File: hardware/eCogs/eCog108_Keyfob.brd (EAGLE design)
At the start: 47.5 x 28 mm, 7 parts

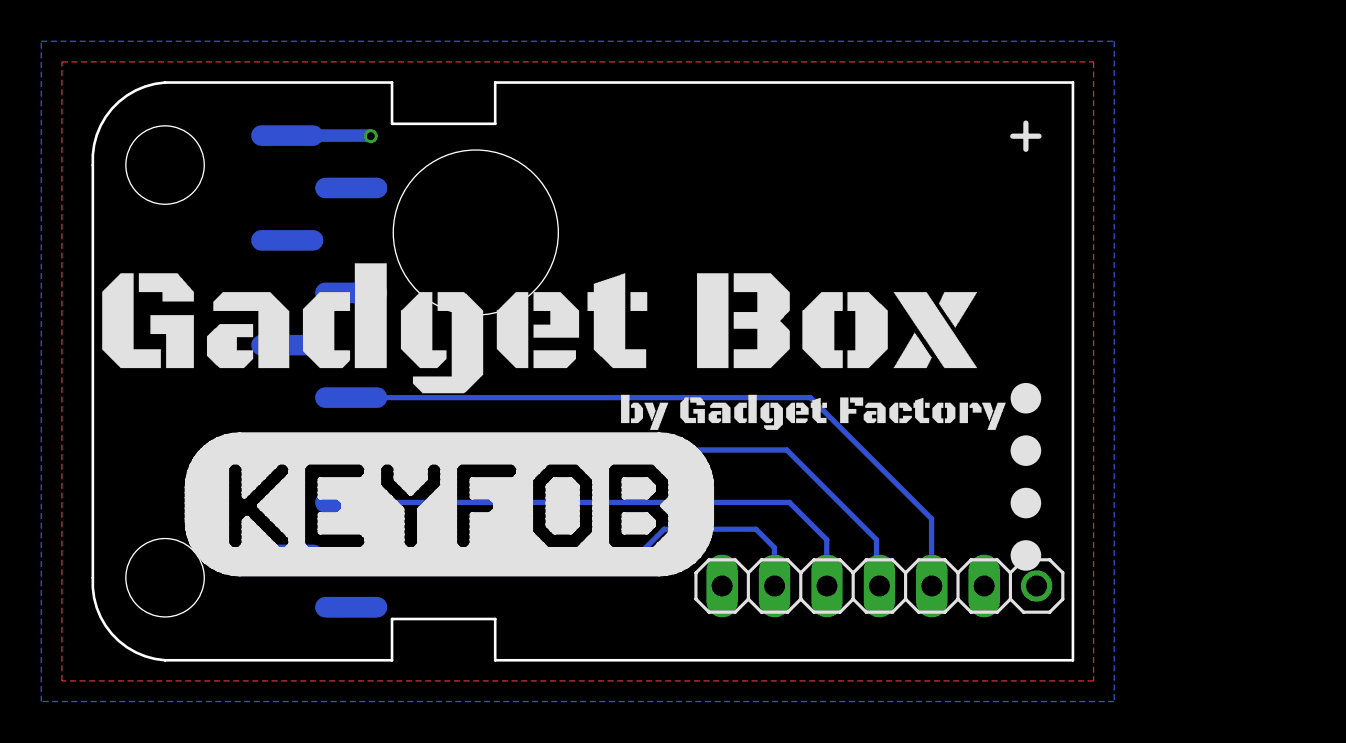
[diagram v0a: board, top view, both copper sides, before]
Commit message: Update eCogs to through hole
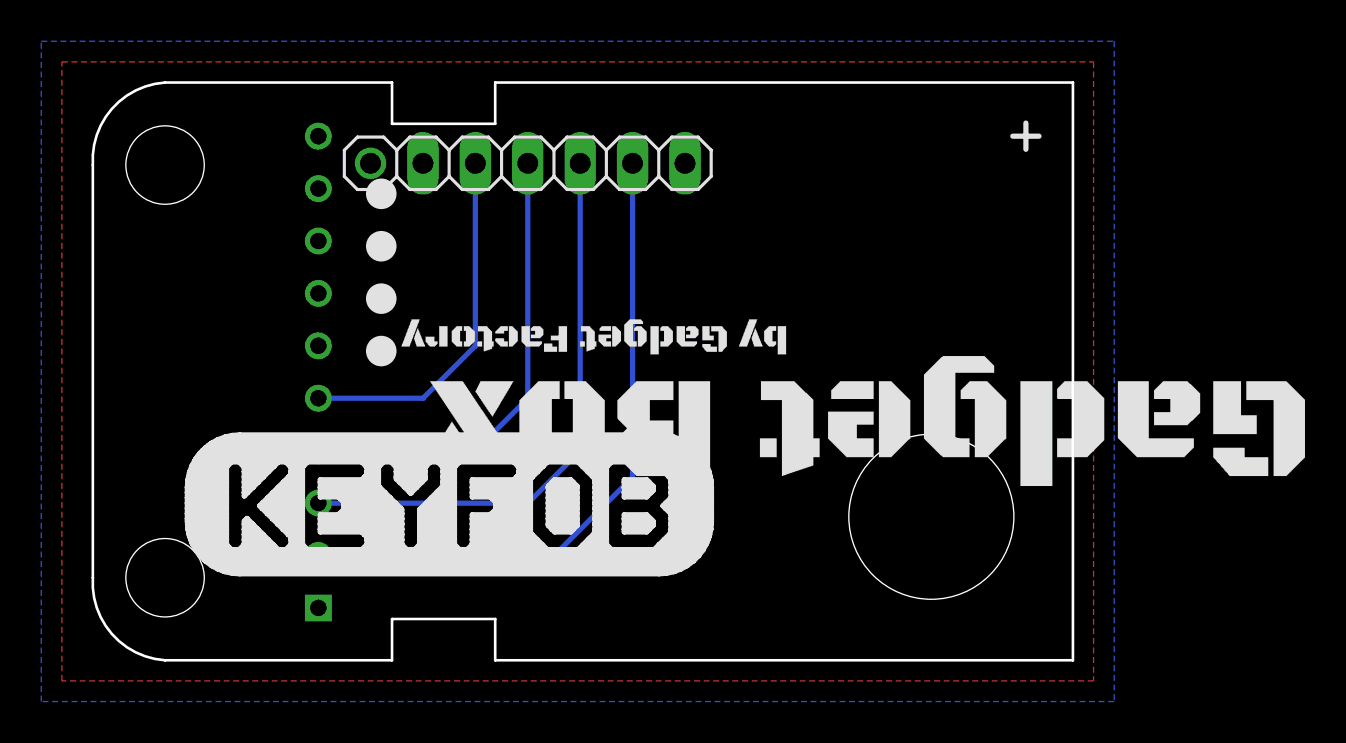
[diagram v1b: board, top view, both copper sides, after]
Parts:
- ECOG: value ECOG_GENERAL_ROWECOG_GENERAL_SMD -> ECOG_GENERAL_ROWTHROUGHOLE; device eCogs:ECOG_GENERAL_SMD -> eCogs:ECOG_GENERAL_TH
- moved U$5 35.8 mm to (14.5, 22.6), turned to 180 degrees
- moved U$4 33.6 mm to (14.5, 20.1), turned to 180 degrees
- moved U$3 32.1 mm to (14.5, 17.5), turned to 180 degrees
- moved U$2 31.3 mm to (14.5, 15.0), turned to 180 degrees
- moved JP1 26.6 mm to (21.6, 24.1), turned to 180 degrees
- moved U$1 16.3 mm to (38.0, 11.8), turned to 180 degrees
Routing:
- net D0: track 33.8 -> 17.5 mm
- net D1: track 32.7 -> 22.6 mm
- net D3: track 26.4 -> 32.0 mm
- net 3V3: track 4.06 -> 0.00 mm, vias 1 -> 0
- net D2: track 26.0 -> 27.7 mm
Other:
- board text added: "XC0"
- board text added: "XC1"
- board text added: "XC2"
- board text added: "XC3"
- board text added: "ecog108 v2.1"
- board text removed: "0"
- board text removed: "1"
- board text removed: "2"
- board text removed: "3"
- board text removed: "ecog108 v2.0"
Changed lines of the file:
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@@
 <layer number="19" name="Unrouted" color="6" fill="1" visible="yes" active="yes"/>
 <layer number="20" name="Dimension" color="15" fill="1" visible="yes" active="yes"/>
-<layer number="21" name="tPlace" color="16" fill="1" visible="yes" active="yes"/>
+<layer number="21" name="tPlace" color="16" fill="1" visible="no" active="yes"/>
 <layer number="22" name="bPlace" color="14" fill="1" visible="yes" active="yes"/>
 <layer number="23" name="tOrigins" color="15" fill="1" visible="yes" active="yes"/>
@@
 <board>
 <plain>
-<text x="43.909" y="22.225" size="0.8128" layer="22" font="vector" rot="MR0">ecog108.GadgetFactory.net</text>
-<text x="42.242" y="12.319" size="1.016" layer="22" font="vector" rot="MR0">ecog108 v2.0</text>
-<text x="42.242" y="13.589" size="1.016" layer="22" font="vector" rot="MR0">Keyfob</text>
-<text x="42.242" y="14.859" size="1.016" layer="22" font="vector" rot="MR0">eCogs</text>
-<text x="17.685" y="7.112" size="1.016" layer="22" font="vector" rot="MR0">D2</text>
-<text x="17.685" y="9.652" size="1.016" layer="22" font="vector" rot="MR0">D1</text>
-<text x="17.685" y="12.192" size="1.016" layer="22" font="vector" rot="MR0">D0</text>
-<text x="17.685" y="4.572" size="1.016" layer="22" font="vector" rot="MR0">D3</text>
-<text x="40.132" y="21.336" size="0.6096" layer="22" font="vector" rot="MR0">Copyright 2016</text>
-<text x="41.862" y="20.447" size="0.6096" layer="22" font="vector" rot="MR0">Gadget Factory, LLC</text>
+<text x="46.703" y="21.717" size="0.8128" layer="22" font="vector" rot="MR0">ecog108.GadgetFactory.net</text>
+<text x="45.036" y="11.811" size="1.016" layer="22" font="vector" rot="MR0">ecog108 v2.1</text>
+<text x="45.036" y="13.081" size="1.016" layer="22" font="vector" rot="MR0">Keyfob</text>
+<text x="45.036" y="14.351" size="1.016" layer="22" font="vector" rot="MR0">eCogs</text>
+<text x="9.938" y="6.985" size="1.016" layer="22" font="vector" rot="MR0">D2</text>
+<text x="9.938" y="9.525" size="1.016" layer="22" font="vector" rot="MR0">D1</text>
+<text x="9.938" y="12.065" size="1.016" layer="22" font="vector" rot="MR0">D0</text>
+<text x="9.938" y="4.445" size="1.016" layer="22" font="vector" rot="MR0">D3</text>
+<text x="42.926" y="20.828" size="0.6096" layer="22" font="vector" rot="MR0">Copyright 2016</text>
+<text x="44.656" y="19.939" size="0.6096" layer="22" font="vector" rot="MR0">Gadget Factory, LLC</text>
 <text x="8.541" y="26.289" size="1.016" layer="22" font="vector" rot="MR0">3.3V</text>
-<text x="17.685" y="2.413" size="1.016" layer="22" font="vector" rot="MR0">GND</text>
-<wire x1="6.06" y1="2" x2="47.06" y2="2" width="0.254" layer="22"/>
-<wire x1="47.06" y1="2" x2="47.06" y2="25" width="0.254" layer="22"/>
-<wire x1="47.06" y1="25" x2="6.06" y2="25" width="0.254" layer="22"/>
-<wire x1="6.06" y1="25" x2="6.06" y2="2" width="0.254" layer="22"/>
-<hole x="19.06" y="20.73" drill="8"/>
+<text x="9.938" y="2.286" size="1.016" layer="22" font="vector" rot="MR0">GND</text>
+<wire x1="54.138" y1="25.686" x2="13.138" y2="25.686" width="0.254" layer="22"/>
+<wire x1="13.138" y1="25.686" x2="13.138" y2="2.686" width="0.254" layer="22"/>
+<wire x1="13.138" y1="2.686" x2="54.138" y2="2.686" width="0.254" layer="22"/>
+<wire x1="54.138" y1="2.686" x2="54.138" y2="25.686" width="0.254" layer="22"/>
+<hole x="41.138" y="6.956" drill="8"/>
 <wire x1="23.6582" y1="6.2196" x2="22.8848" y2="6.2196" width="0.254" layer="21"/>
 <wire x1="22.8848" y1="6.2196" x2="22.7544" y2="6.35" width="0.254" layer="21"/>
@@
 <wire x1="6.1068" y1="10.414" x2="29.4532" y2="10.414" width="0.254" layer="21"/>
 <wire x1="6.52" y1="10.668" x2="29.04" y2="10.668" width="0.254" layer="21"/>
-<text x="7.906" y="4.572" size="1.016" layer="22" font="vector" rot="MR0">0</text>
+<text x="8.287" y="5.08" size="1.016" layer="22" font="vector" rot="MR0">XC0</text>
 <wire x1="45.72" y1="26.035" x2="45.72" y2="24.765" width="0.254" layer="21"/>
 <wire x1="45.085" y1="25.4" x2="46.355" y2="25.4" width="0.254" layer="21"/>
-<text x="7.906" y="7.112" size="1.016" layer="22" font="vector" rot="MR0">1</text>
-<text x="7.906" y="9.652" size="1.016" layer="22" font="vector" rot="MR0">2</text>
-<text x="7.906" y="12.192" size="1.016" layer="22" font="vector" rot="MR0">3</text>
+<text x="7.779" y="6.985" size="1.016" layer="22" font="vector" rot="MR0">XC1</text>
+<text x="7.779" y="9.525" size="1.016" layer="22" font="vector" rot="MR0">XC2</text>
+<text x="7.779" y="12.065" size="1.016" layer="22" font="vector" rot="MR0">XC3</text>
 </plain>
 <attributes>
@@
 </autorouter>
 <elements>
-<element name="ECOG" library="eCogs" package="ECOG_GENERAL_SMD" value="ECOG_GENERAL_ROWECOG_GENERAL_SMD" x="0" y="0" smashed="yes">
-<attribute name="DIGIKEY" value="S1013EC-10-ND" x="0" y="0" size="1.778" layer="27" display="off"/>
+<element name="ECOG" library="eCogs" package="ECOG_GENERAL_TH" value="ECOG_GENERAL_ROWTHROUGHOLE" x="0" y="0" smashed="yes"/>
+<element name="U$2" library="eCogs" package="LEGEND_DIO" value="" x="14.478" y="14.986" rot="R180"/>
+<element name="U$3" library="eCogs" package="LEGEND_DIO" value="" x="14.478" y="17.526" rot="R180"/>
+<element name="JP1" library="pinhead" package="1X07" value="" x="21.578" y="24.086" smashed="yes" rot="R180">
+<attribute name="VALUE" x="30.468" y="27.261" size="1.27" layer="27" rot="R180"/>
 </element>
-<element name="U$2" library="eCogs" package="LEGEND_DIO" value="" x="45.72" y="12.7"/>
-<element name="U$3" library="eCogs" package="LEGEND_DIO" value="" x="45.72" y="10.16"/>
-<element name="JP1" library="pinhead" package="1X07" value="" x="38.62" y="3.6" smashed="yes">
-<attribute name="VALUE" x="29.73" y="0.425" size="1.27" layer="27"/>
-</element>
-<element name="U$4" library="eCogs" package="LEGEND_DIO" value="" x="45.72" y="7.62"/>
-<element name="U$5" library="eCogs" package="LEGEND_DIO" value="" x="45.72" y="5.08"/>
-<element name="U$1" library="GadgetFactory" package="GADGETBOX_TEXT" value="" x="22.225" y="15.875"/>
+<element name="U$4" library="eCogs" package="LEGEND_DIO" value="" x="14.478" y="20.066" rot="R180"/>
+<element name="U$5" library="eCogs" package="LEGEND_DIO" value="" x="14.478" y="22.606" rot="R180"/>
+<element name="U$1" library="GadgetFactory" package="GADGETBOX_TEXT" value="" x="37.973" y="11.811" rot="R180"/>
 </elements>
 <signals>
@@
 </polygon>
 <contactref element="JP1" pad="6"/>
-<wire x1="9.92324375" y1="25.429" x2="13.941" y2="25.429" width="0.6096" layer="16"/>
-<wire x1="13.941" y1="25.429" x2="13.97" y2="25.4" width="0.6096" layer="16"/>
-<via x="13.97" y="25.4" extent="1-16" drill="0.381"/>
 </signal>
 <signal name="D3">
 <contactref element="JP1" pad="2"/>
 <contactref element="ECOG" pad="G0"/>
-<wire x1="9.92324375" y1="5.1110625" x2="26.9550625" y2="5.1110625" width="0.254" layer="16"/>
-<wire x1="26.9550625" y1="5.1110625" x2="28.194" y2="6.35" width="0.254" layer="16"/>
-<wire x1="28.194" y1="6.35" x2="32.639" y2="6.35" width="0.254" layer="16"/>
-<wire x1="32.639" y1="6.35" x2="33.528" y2="5.461" width="0.254" layer="16"/>
-<wire x1="33.528" y1="5.461" x2="33.528" y2="3.612" width="0.254" layer="16"/>
-<wire x1="33.528" y1="3.612" x2="33.54" y2="3.6" width="0.254" layer="16"/>
+<wire x1="26.658" y1="24.086" x2="26.658" y2="8.878" width="0.254" layer="16"/>
+<wire x1="26.658" y1="8.878" x2="22.86" y2="5.08" width="0.254" layer="16"/>
+<wire x1="22.86" y1="5.08" x2="11.43" y2="5.08" width="0.254" layer="16"/>
 </signal>
 <signal name="D2">
 <contactref element="JP1" pad="3"/>
 <contactref element="ECOG" pad="G1"/>
-<wire x1="13.02204375" y1="7.649" x2="34.261" y2="7.649" width="0.254" layer="16"/>
-<wire x1="34.261" y1="7.649" x2="36.068" y2="5.842" width="0.254" layer="16"/>
-<wire x1="36.068" y1="5.842" x2="36.068" y2="3.612" width="0.254" layer="16"/>
-<wire x1="36.068" y1="3.612" x2="36.08" y2="3.6" width="0.254" layer="16"/>
+<wire x1="24.118" y1="24.086" x2="24.118" y2="10.148" width="0.254" layer="16"/>
+<wire x1="24.118" y1="10.148" x2="21.59" y2="7.62" width="0.254" layer="16"/>
+<wire x1="21.59" y1="7.62" x2="11.43" y2="7.62" width="0.254" layer="16"/>
 </signal>
 <signal name="D1">
 <contactref element="JP1" pad="4"/>
 <contactref element="ECOG" pad="G2"/>
-<wire x1="9.92324375" y1="10.189" x2="34.134" y2="10.189" width="0.254" layer="16"/>
-<wire x1="34.134" y1="10.189" x2="38.481" y2="5.842" width="0.254" layer="16"/>
-<wire x1="38.481" y1="5.842" x2="38.481" y2="3.739" width="0.254" layer="16"/>
-<wire x1="38.481" y1="3.739" x2="38.62" y2="3.6" width="0.254" layer="16"/>
+<wire x1="21.578" y1="24.086" x2="21.578" y2="12.688" width="0.254" layer="16"/>
+<wire x1="21.578" y1="12.688" x2="19.05" y2="10.16" width="0.254" layer="16"/>
+<wire x1="19.05" y1="10.16" x2="11.43" y2="10.16" width="0.254" layer="16"/>
 </signal>
 <signal name="D0">
 <contactref element="JP1" pad="5"/>
 <contactref element="ECOG" pad="G3"/>
-<wire x1="13.02204375" y1="12.729" x2="35.277" y2="12.729" width="0.254" layer="16"/>
-<wire x1="35.277" y1="12.729" x2="41.148" y2="6.858" width="0.254" layer="16"/>
-<wire x1="41.148" y1="6.858" x2="41.148" y2="3.612" width="0.254" layer="16"/>
-<wire x1="41.148" y1="3.612" x2="41.16" y2="3.6" width="0.254" layer="16"/>
+<wire x1="19.038" y1="24.086" x2="19.038" y2="15.228" width="0.254" layer="16"/>
+<wire x1="19.038" y1="15.228" x2="16.51" y2="12.7" width="0.254" layer="16"/>
+<wire x1="16.51" y1="12.7" x2="11.43" y2="12.7" width="0.254" layer="16"/>
 </signal>
 </signals>
